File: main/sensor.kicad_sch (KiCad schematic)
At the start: 4 parts, among them U6 Pico, U7 Waveshare 3945, U8 VL53L0X

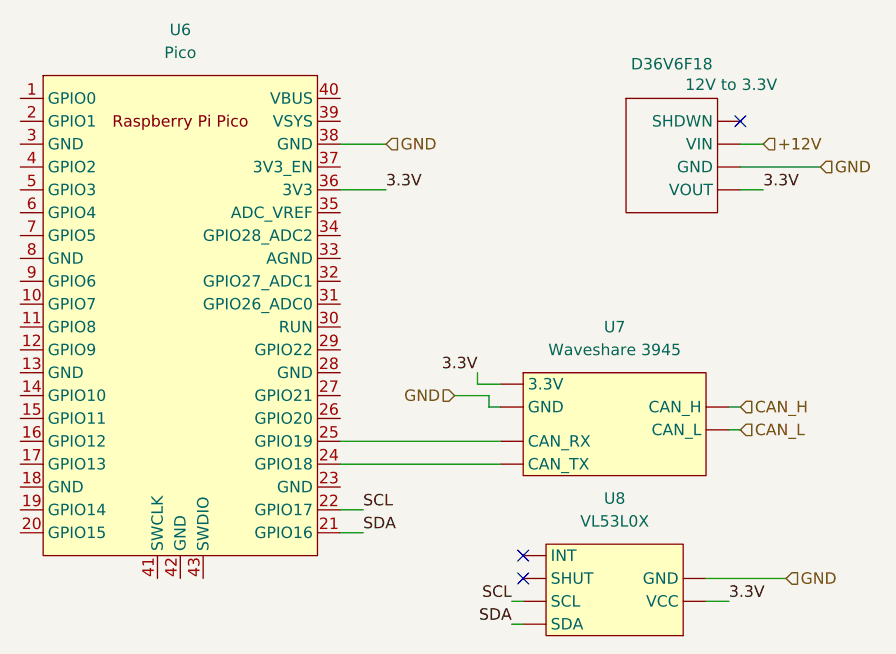
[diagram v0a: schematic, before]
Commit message: Added control motor module
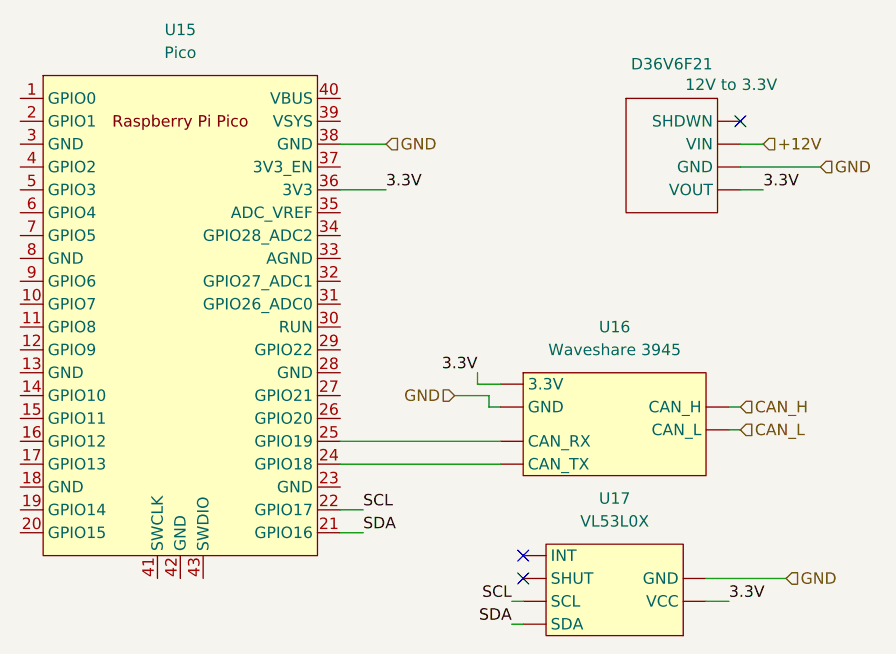
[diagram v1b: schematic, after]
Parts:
- renumbered D36V6F18 to D36V6F21, U6 to U15, U7 to U16, U8 to U17
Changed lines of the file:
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@@
 		(dnp no)
 		(fields_autoplaced yes)
-		(property "Reference" "U8"
+		(property "Reference" "U17"
 			(at 109.22 73.66 0)
 			(effects
@@
 				(path "/54fbbba9-a737-4199-9a4b-f9fa49b3de5e/956e0365-6d74-4799-9d68-b1a004ee179e/691d0288-4a08-47b2-8436-3e4c1f0c1747"
 					(reference "U11")
+					(unit 1)
+				)
+				(path "/54fbbba9-a737-4199-9a4b-f9fa49b3de5e/956e0365-6d74-4799-9d68-b1a004ee179e/6bee5958-45a1-4a7d-a0c1-aebf48de0034"
+					(reference "U?")
 					(unit 1)
 				)
@@
 		(on_board yes)
 		(dnp no)
-		(property "Reference" "D36V6F18"
+		(property "Reference" "D36V6F21"
 			(at 115.57 25.4 0)
 			(effects
@@
 				(path "/54fbbba9-a737-4199-9a4b-f9fa49b3de5e/956e0365-6d74-4799-9d68-b1a004ee179e/691d0288-4a08-47b2-8436-3e4c1f0c1747"
 					(reference "D36V6F19")
+					(unit 1)
+				)
+				(path "/54fbbba9-a737-4199-9a4b-f9fa49b3de5e/956e0365-6d74-4799-9d68-b1a004ee179e/6bee5958-45a1-4a7d-a0c1-aebf48de0034"
+					(reference "D36V6F?")
 					(unit 1)
 				)
@@
 		(dnp no)
 		(fields_autoplaced yes)
-		(property "Reference" "U7"
+		(property "Reference" "U16"
 			(at 109.22 54.61 0)
 			(effects
@@
 				(path "/54fbbba9-a737-4199-9a4b-f9fa49b3de5e/956e0365-6d74-4799-9d68-b1a004ee179e/691d0288-4a08-47b2-8436-3e4c1f0c1747"
 					(reference "U10")
+					(unit 1)
+				)
+				(path "/54fbbba9-a737-4199-9a4b-f9fa49b3de5e/956e0365-6d74-4799-9d68-b1a004ee179e/6bee5958-45a1-4a7d-a0c1-aebf48de0034"
+					(reference "U?")
 					(unit 1)
 				)
@@
 		(dnp no)
 		(fields_autoplaced yes)
-		(property "Reference" "U6"
+		(property "Reference" "U15"
 			(at 60.96 21.59 0)
 			(effects
@@
 					(unit 1)
 				)
+				(path "/54fbbba9-a737-4199-9a4b-f9fa49b3de5e/956e0365-6d74-4799-9d68-b1a004ee179e/6bee5958-45a1-4a7d-a0c1-aebf48de0034"
+					(reference "U?")
+					(unit 1)
+				)

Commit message: added logos, oranised sheets, final version
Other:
- company: (none) -> Designers: Krzysztof Grajek, Wojtek Kołodziej
